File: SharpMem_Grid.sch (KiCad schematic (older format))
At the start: 39 parts, among them J1 CONN_01X05, J2 CONN_01X01, J3 CONN_01X01, J4 USB_B_Micro, SW1 PTS810_SJK_250_SMTR_LFS, SW2 PTS810_SJK_250_SMTR_LFS, U1 25LC_EEPROM, U2 Schmitt_Inverter_Single, U3 PIC32MX250F128B-I/SS, U4 TLV76033DBZR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

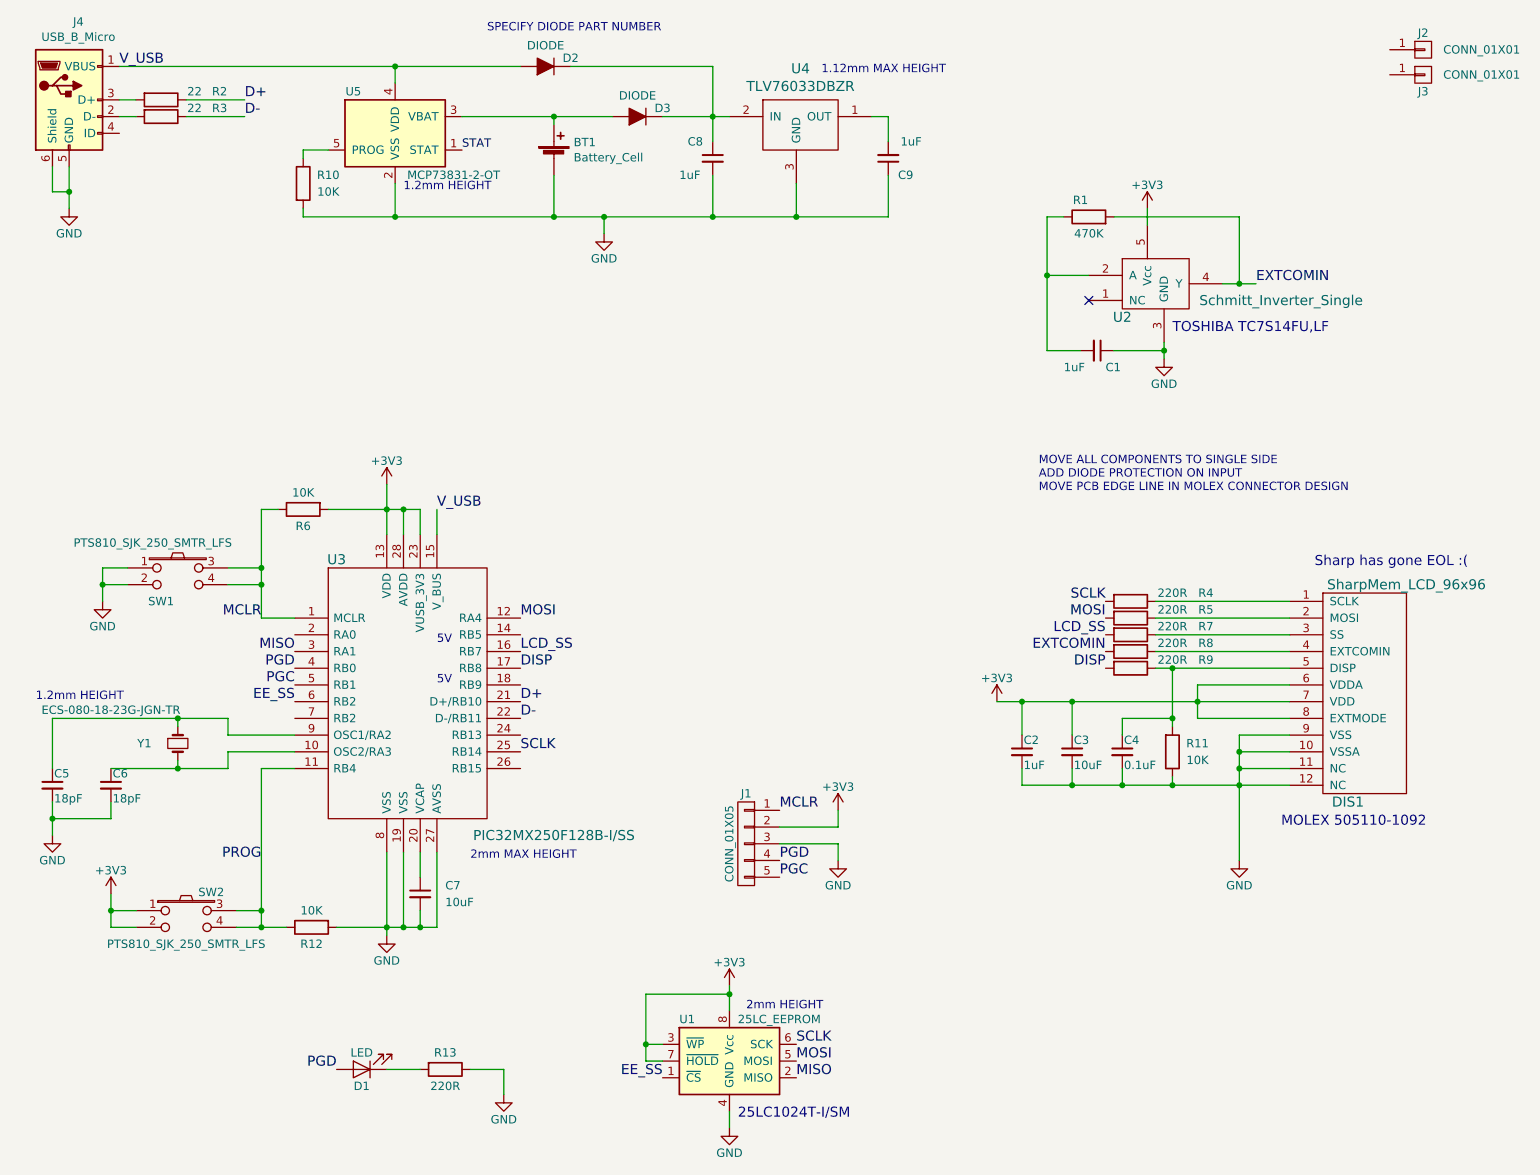
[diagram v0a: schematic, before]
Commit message: board layout and routing passing DRC
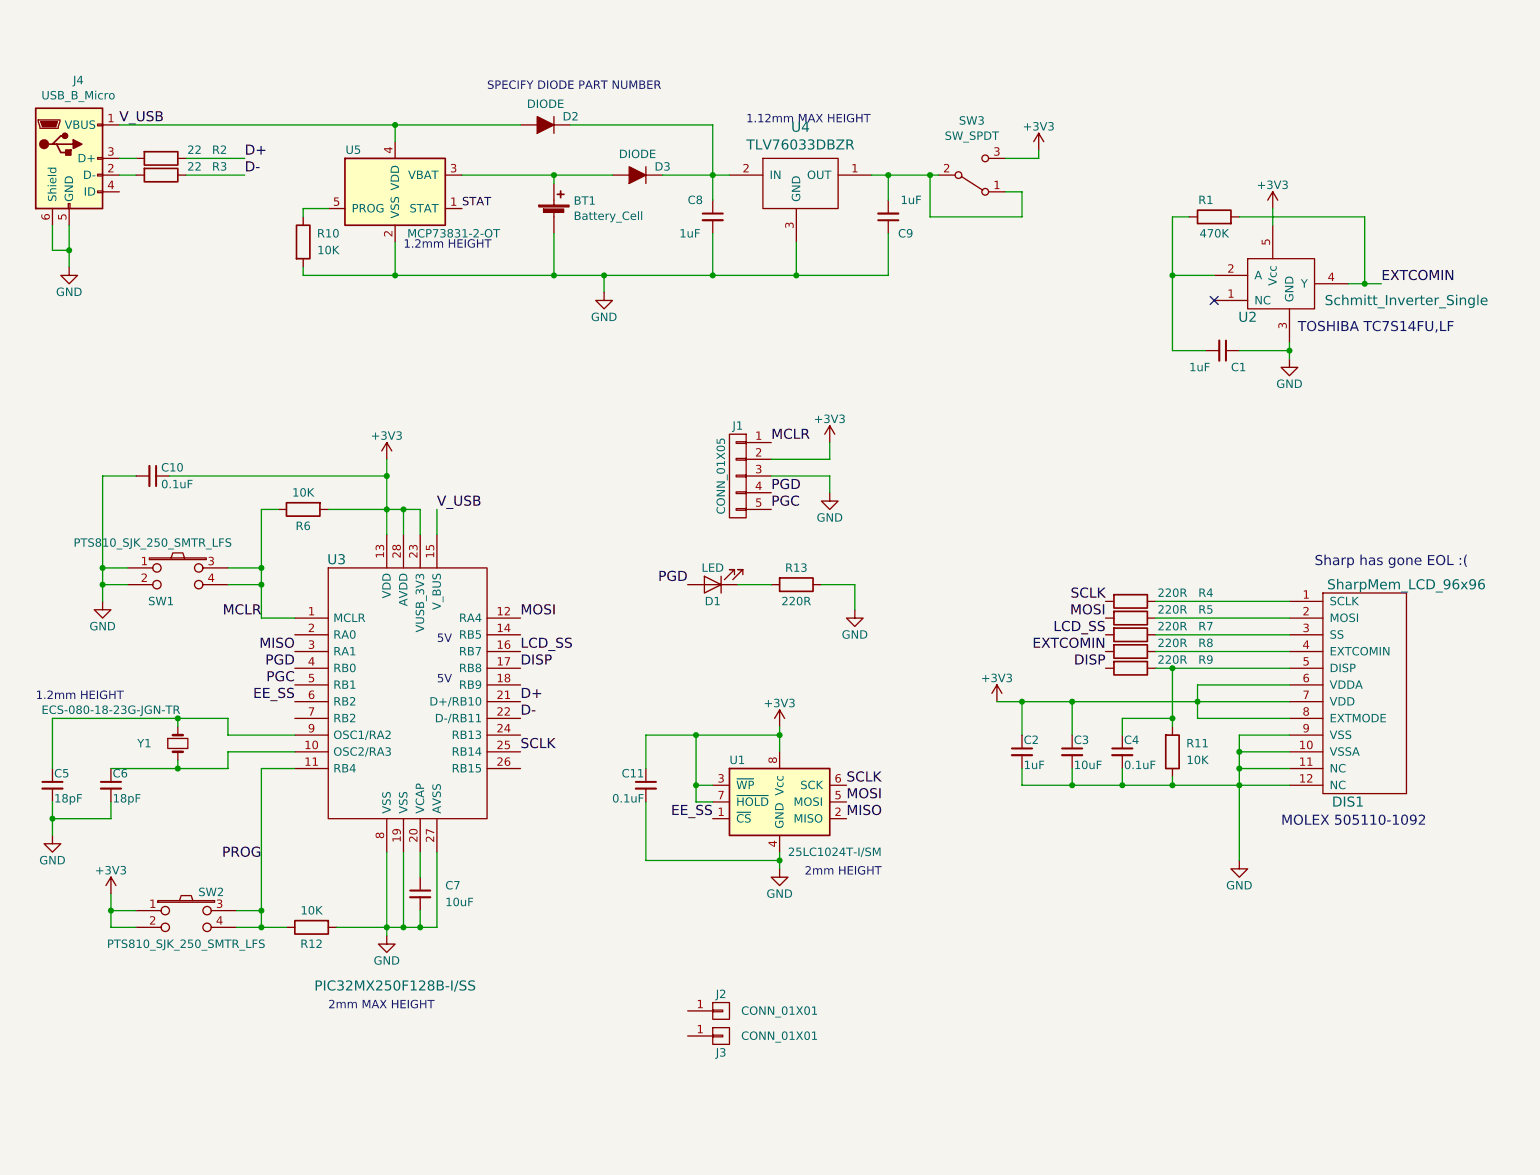
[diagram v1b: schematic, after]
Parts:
- added C10, C11: 0.1uF, Capacitors_SMD:C_0603, symbol Device:C_Small
- added SW3: SW_SPDT, Solutions:SSSS810701_ALPS_SPDT, symbol Switch:SW_SPDT
- U1: value 25LC_EEPROM -> 25LC1024T-I/SM
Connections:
- net +3V3: now also C10.1, C11.1, SW3.3 (C)
- net GND: now also C10.2, C11.2
- net at C9.2, U4.1 (OUT): now also SW3.1 (A), SW3.2 (B)
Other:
- note removed: "25LC1024T-I/SM\n"
- note removed: "MOVE ALL COMPONENTS TO SINGLE SIDE\nADD DIODE PROTECTION ON INPUT\nMOVE PCB EDGE LINE IN MOLEX CONNECTOR DESIGN"
- moved on the sheet: BT1, C1, C8, C9, D1, D2, D3, J1, J2, J3, J4, R1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

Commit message: schematic
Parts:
- D2, D3: value DIODE -> CDBU0130L
- DIS1: value SharpMem_LCD_96x96 -> 505110-1092
- SW3: value SW_SPDT -> SSSS810701
- U2: value Schmitt_Inverter_Single -> TC7S14FU,LF
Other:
- note added: "MOLEX \n"
- note removed: "MOLEX 505110-1092\n\n"
- note removed: "SPECIFY DIODE PART NUMBER"
- note removed: "TOSHIBA TC7S14FU,LF"
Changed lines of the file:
@@
 P 8500 4050
 F 0 "DIS1" H 8850 2650 60  0000 C CNN
-F 1 "SharpMem_LCD_96x96" H 9200 3950 60  0000 C CNN
+F 1 "505110-1092" H 9200 3950 60  0000 C CNN
 F 2 "Solutions:MOLEX_505110-1092" H 8500 4050 60  0001 C CNN
 F 3 "" H 8500 4050 60  0000 C CNN
@@
 	1    0    0    -1
 $EndComp
-Text Notes 8550 2650 0    60   ~ 0
-TOSHIBA TC7S14FU,LF
 Text Notes 8650 4050 0    60   ~ 0
 Sharp has gone EOL :(
@@
 	1    0    0    -1
 $EndComp
-Text Notes 8450 5700 0    60   ~ 0
-MOLEX 505110-1092\n\n
+Text Notes 9250 4350 0    60   ~ 0
+MOLEX \n
 $Comp
 L Device:R R4
@@
 P 8650 2350
 F 0 "U2" H 8250 2150 60  0000 C CNN
-F 1 "Schmitt_Inverter_Single" H 9200 2250 60  0000 C CNN
+F 1 "TC7S14FU,LF" H 9200 2250 60  0000 C CNN
 F 2 "Solutions:SSOP-5-0.65_PITCH" H 8650 2350 60  0001 C CNN
 F 3 "" H 8650 2350 60  0000 C CNN
@@
 P 4050 1400
 F 0 "D2" H 3900 1350 50  0000 C CNN
-F 1 "DIODE" H 4050 1275 50  0000 C CNN
+F 1 "CDBU0130L" H 4050 1275 50  0000 C CNN
 F 2 "Diodes_SMD:D_0603" H 4050 1400 50  0001 C CNN
 F 3 "~" H 4050 1400 50  0001 C CNN
@@
 P 4600 1700
 F 0 "D3" H 4450 1650 50  0000 C CNN
-F 1 "DIODE" H 4600 1575 50  0000 C CNN
+F 1 "CDBU0130L" H 4600 1575 50  0000 C CNN
 F 2 "Diodes_SMD:D_0603" H 4600 1700 50  0001 C CNN
 F 3 "~" H 4600 1700 50  0001 C CNN
@@
 	4450 1700 4100 1700
 Connection ~ 4100 1700
-Text Notes 3700 1200 0    50   ~ 0
-SPECIFY DIODE PART NUMBER
 Text Notes 2750 6700 0    50   ~ 0
 2mm MAX HEIGHT
@@
 Text Notes 5600 5900 0    50   ~ 0
 2mm HEIGHT
-Text Notes 3200 2150 0    50   ~ 0
+Text Notes 3200 1550 0    50   ~ 0
 1.2mm HEIGHT
 $Comp
@@
 P 6600 1700
 F 0 "SW3" H 6600 1375 50  0000 C CNN
-F 1 "SW_SPDT" H 6600 1466 50  0000 C CNN
+F 1 "SSSS810701" H 6600 1466 50  0000 C CNN
 F 2 "Solutions:SSSS810701_ALPS_SPDT" H 6600 1700 50  0001 C CNN
 F 3 "" H 6600 1700 50  0001 C CNN
